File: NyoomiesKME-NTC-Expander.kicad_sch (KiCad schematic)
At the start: 9 parts, among them J1 2x4 Dupont Socket, J2 JST XH 2 Pin, J3 JST XH 2 Pin, J4 JST XH 2 Pin, J5 JST XH 2 Pin

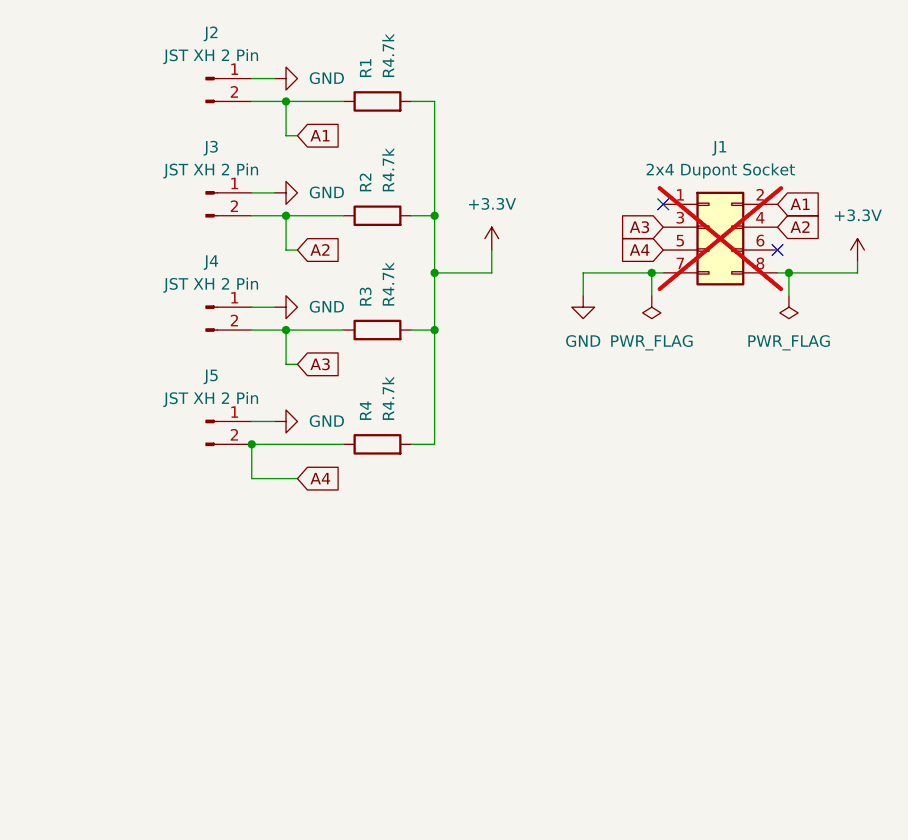
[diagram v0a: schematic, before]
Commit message: rev 0.2: add filter caps
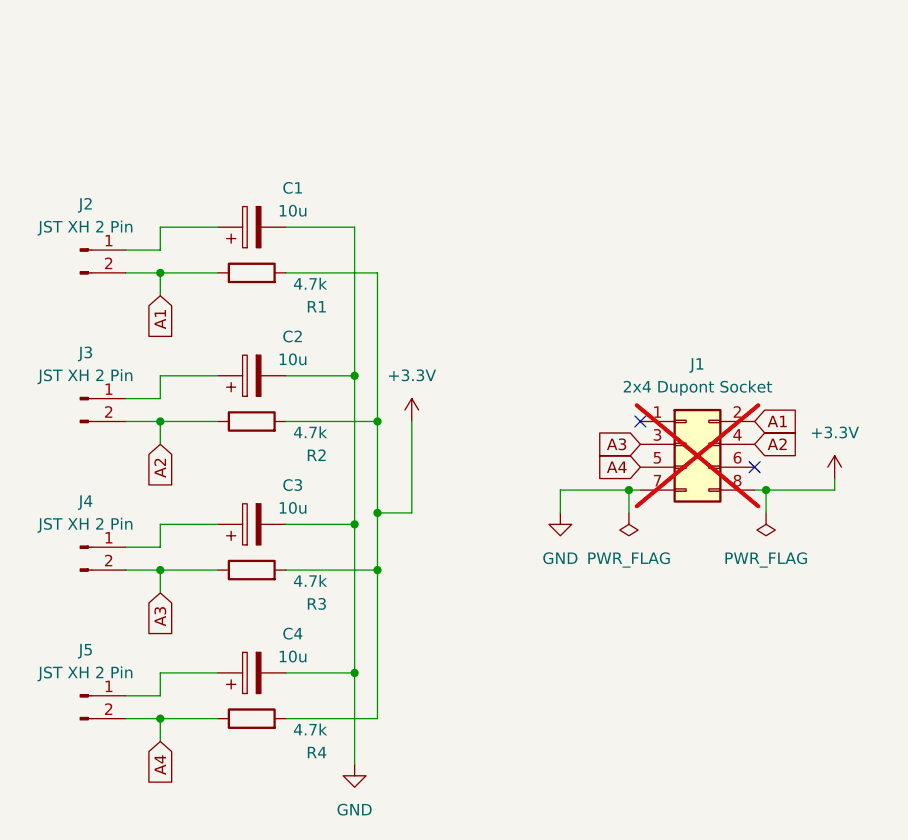
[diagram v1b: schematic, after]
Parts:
- added C1, C2, C3, C4: 10u, Capacitor_SMD:C_1206_3216Metric, symbol Device:C_Polarized
- R1, R2, R3, R4: value R4.7k -> 4.7k
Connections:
- net GND: now also C1.2, C2.2, C3.2, C4.2; no longer J2.1 (Pin_1), J3.1 (Pin_1), J4.1 (Pin_1), J5.1 (Pin_1)
- new net: C2.1, J3.1 (Pin_1)
- new net: C4.1, J5.1 (Pin_1)
- new net: C1.1, J2.1 (Pin_1)
- new net: C3.1, J4.1 (Pin_1)
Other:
- company: (none) -> Philipp Molitor
- title: (none) -> Nyoomies TH Expander
- moved on the sheet: J1, J2, J3, J4, J5, R1, R2, R3, R4

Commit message: switch to 2.2k, fix pcb DRC
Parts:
- R1, R2, R3, R4: value 4.7k -> 2.2k; LCSC Part # C17936 -> C311944
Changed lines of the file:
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@@
 			)
 		)
-		(property "Value" "4.7k"
+		(property "Value" "2.2k"
 			(at 134.112 78.74 90)
 			(effects
@@
 			)
 		)
-		(property "LCSC Part #" "C17936"
+		(property "LCSC Part #" "C311944"
 			(at 125.73 77.47 0)
 			(effects
@@
 			)
 		)
-		(property "Value" "4.7k"
+		(property "Value" "2.2k"
 			(at 134.112 95.25 90)
 			(effects
@@
 			)
 		)
-		(property "LCSC Part #" "C17936"
+		(property "LCSC Part #" "C311944"
 			(at 125.73 93.98 0)
 			(effects
@@
 			)
 		)
-		(property "Value" "4.7k"
+		(property "Value" "2.2k"
 			(at 134.112 128.27 90)
 			(effects
@@
 			)
 		)
-		(property "LCSC Part #" "C17936"
+		(property "LCSC Part #" "C311944"
 			(at 125.73 127 0)
 			(effects
@@
 			)
 		)
-		(property "Value" "4.7k"
+		(property "Value" "2.2k"
 			(at 134.112 111.76 90)
 			(effects
@@
 			)
 		)
-		(property "LCSC Part #" "C17936"
+		(property "LCSC Part #" "C311944"
 			(at 125.73 110.49 0)
 			(effects
